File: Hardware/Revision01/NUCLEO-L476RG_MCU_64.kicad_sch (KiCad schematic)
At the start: 56 parts, among them U10 MCU_LQFP64, X2 ABS25-32.768KHZ-6-T, X3 8MHz(16pF)[N/A]

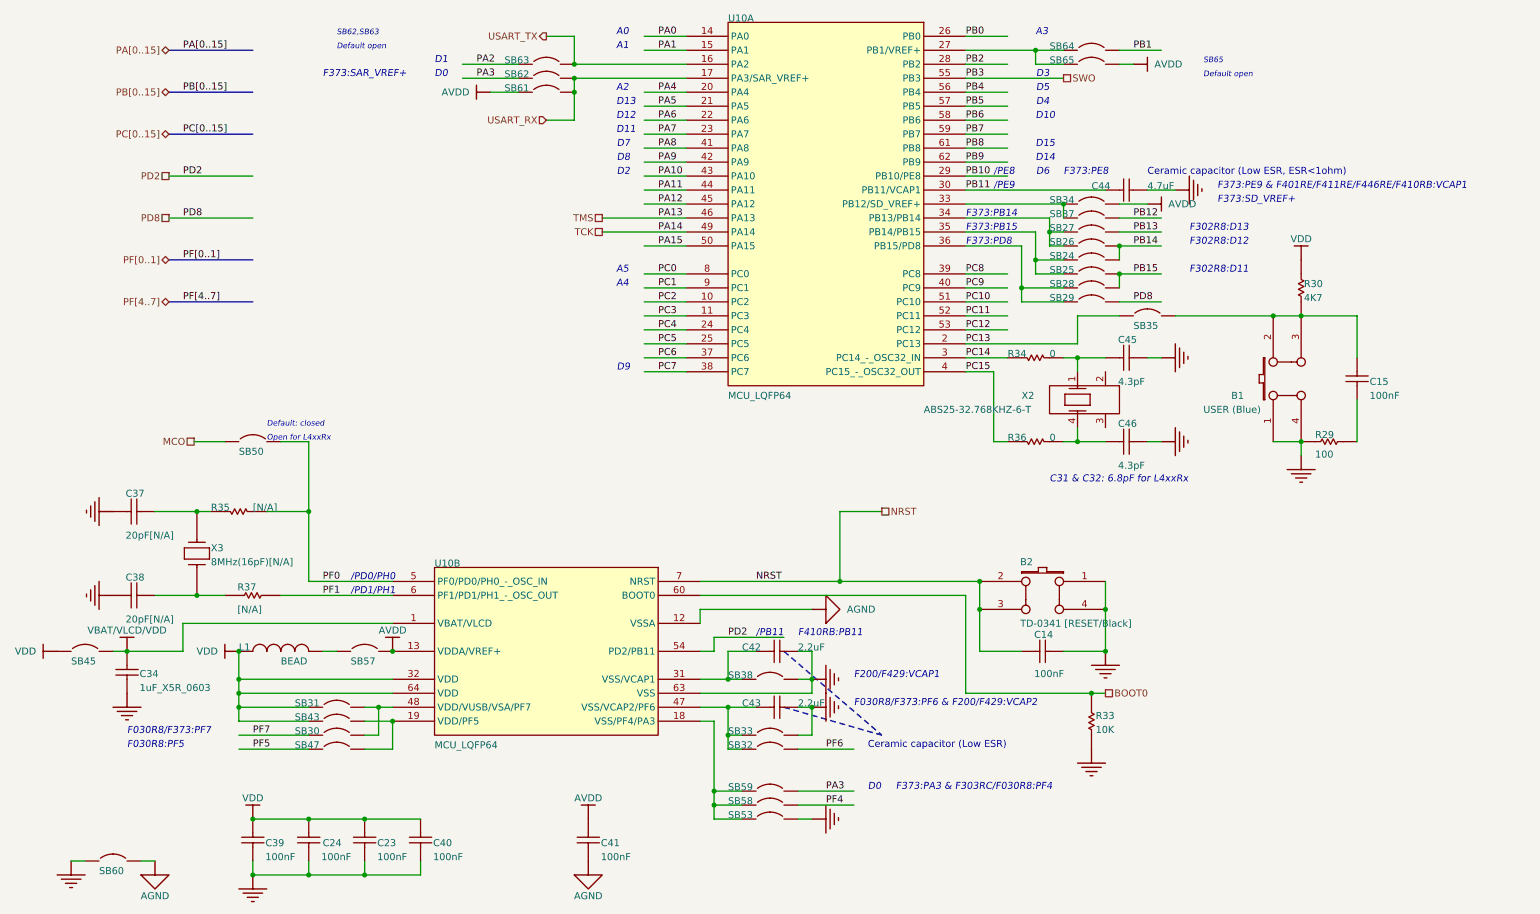
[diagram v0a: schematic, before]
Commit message: . Renamed schematic files, removed old symbol files
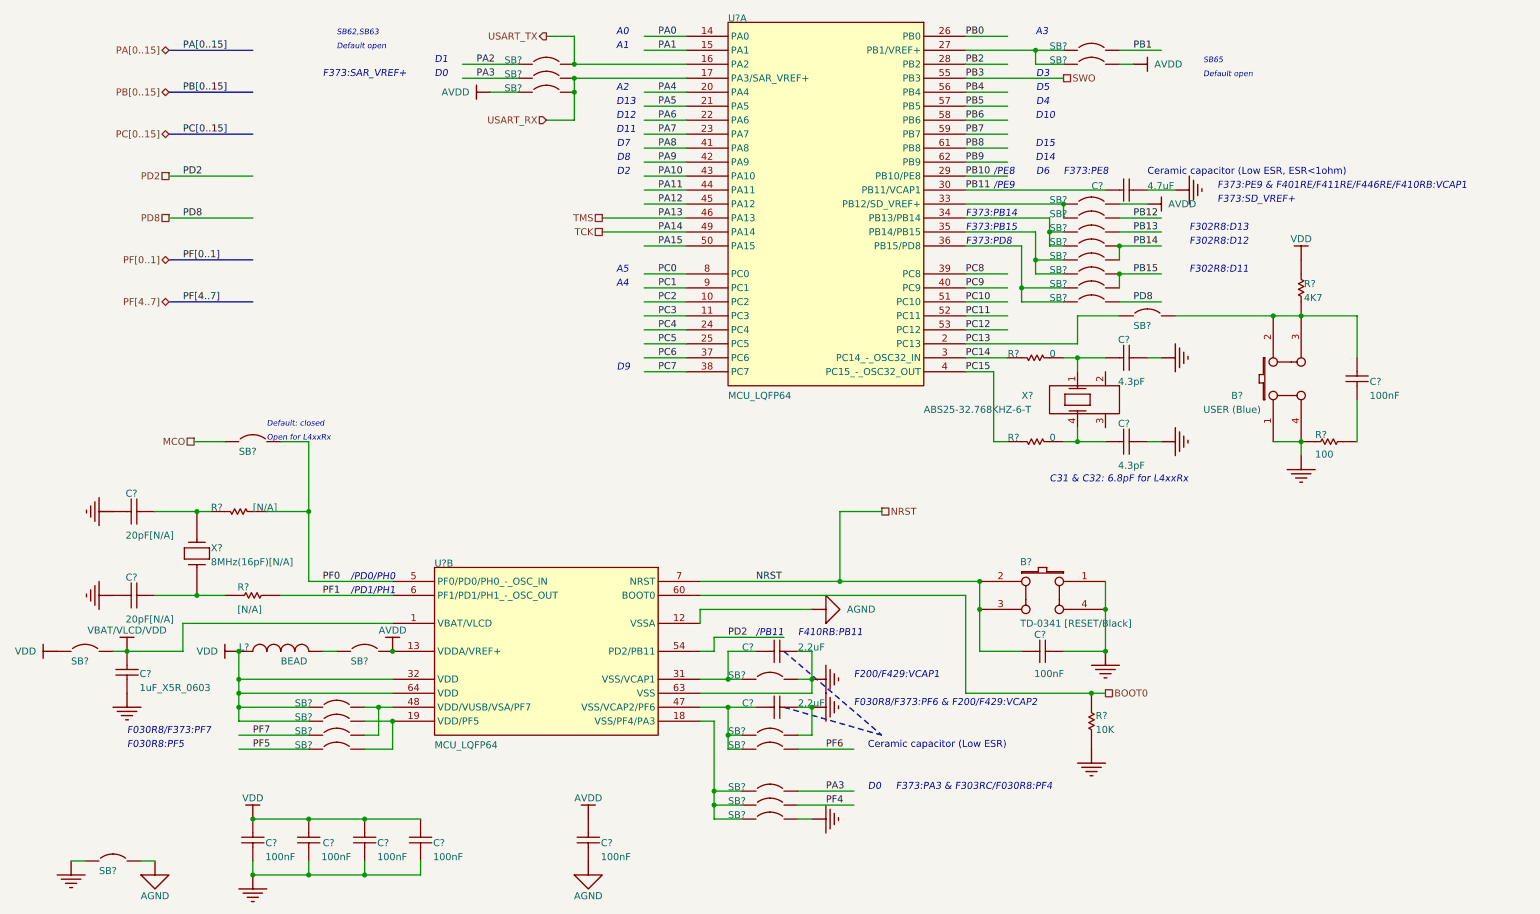
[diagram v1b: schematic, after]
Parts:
- renumbered B2 to B?, B1 to B?, C37 to C?, C45 to C?, C44 to C?, C39 to C?, C34 to C?, C46 to C?, C43 to C?, C14 to C?, C41 to C?, C15 to C?, C24 to C?, C40 to C?, C38 to C?, C23 to C?, C42 to C?, L1 to L?, R29 to R?, R37 to R?, R35 to R?, R34 to R?, R36 to R?, R33 to R?, R30 to R?, SB32 to SB?, SB61 to SB?, SB59 to SB?, SB25 to SB?, SB31 to SB?, SB37 to SB?, SB29 to SB?, SB63 to SB?, SB50 to SB?, SB38 to SB?, SB30 to SB?, SB35 to SB?, SB64 to SB?, SB58 to SB?, SB45 to SB?, SB33 to SB?, SB43 to SB?, SB57 to SB?, SB62 to SB?, SB28 to SB?, SB26 to SB?, SB60 to SB?, SB27 to SB?, SB53 to SB?, SB65 to SB?, SB47 to SB?, SB34 to SB?, SB24 to SB?, U10 to U?, X2 to X?, X3 to X?

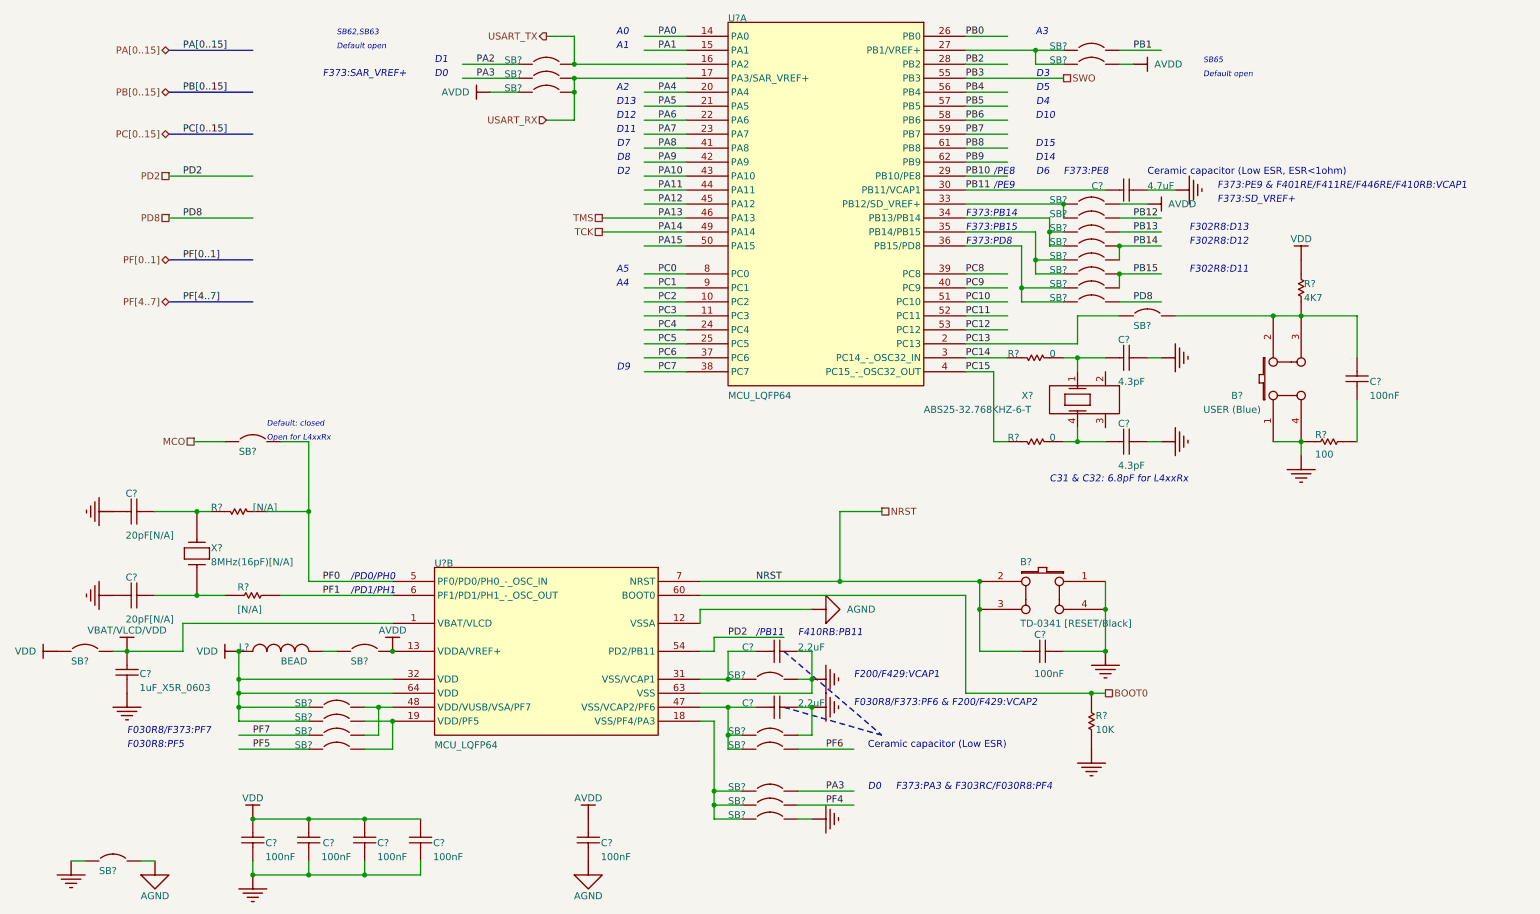
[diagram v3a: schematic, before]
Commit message: . Completed MCU schematic & imported hierarchical model pins
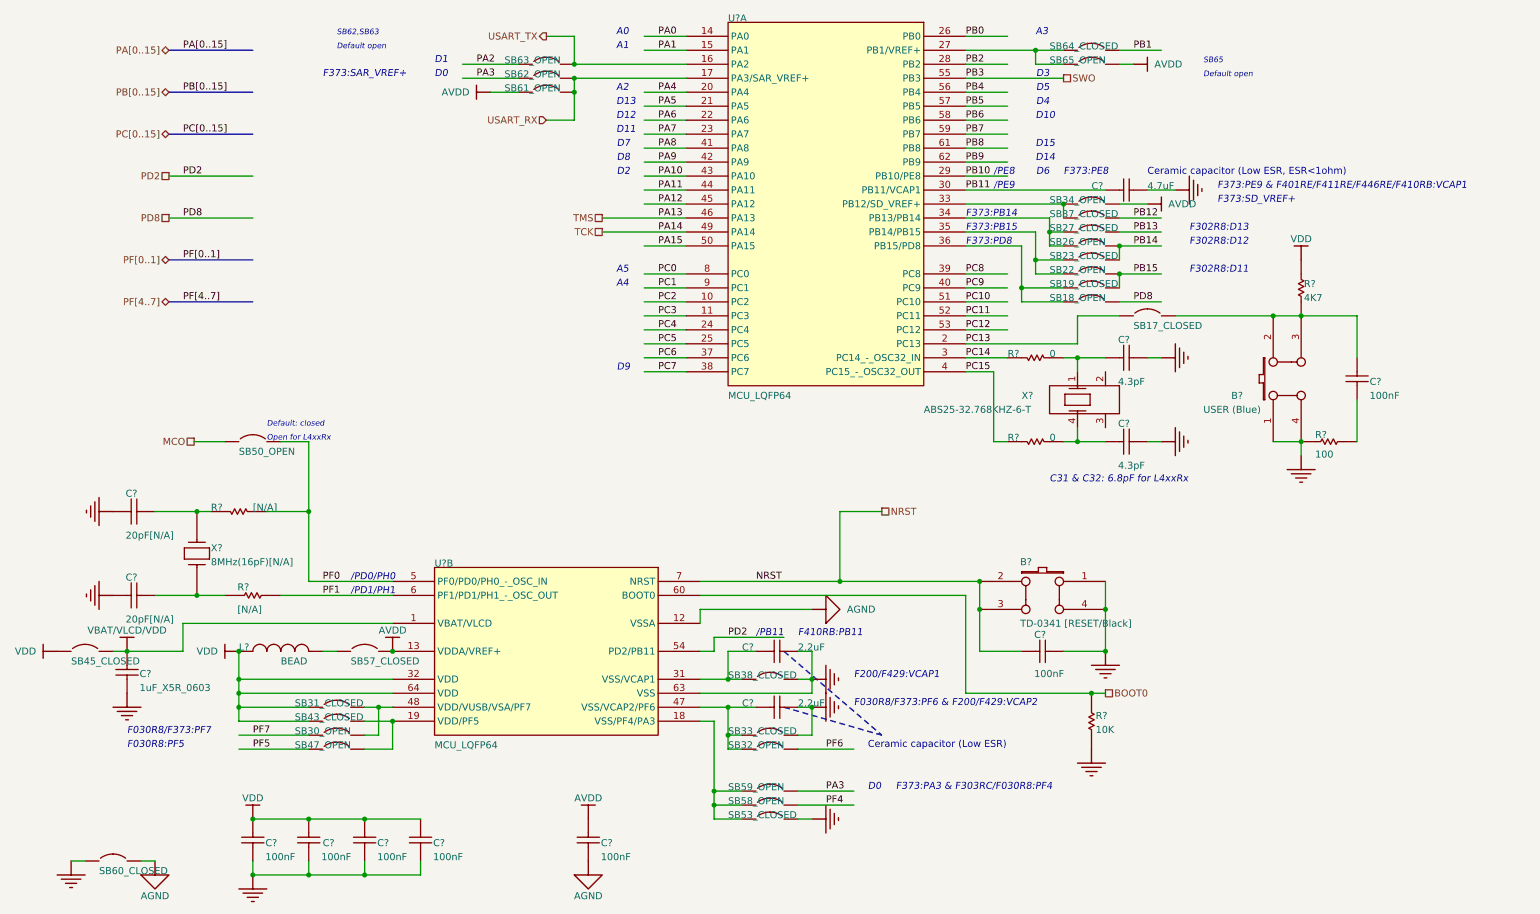
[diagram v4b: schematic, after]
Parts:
- gave numbers to parts that had none: 28

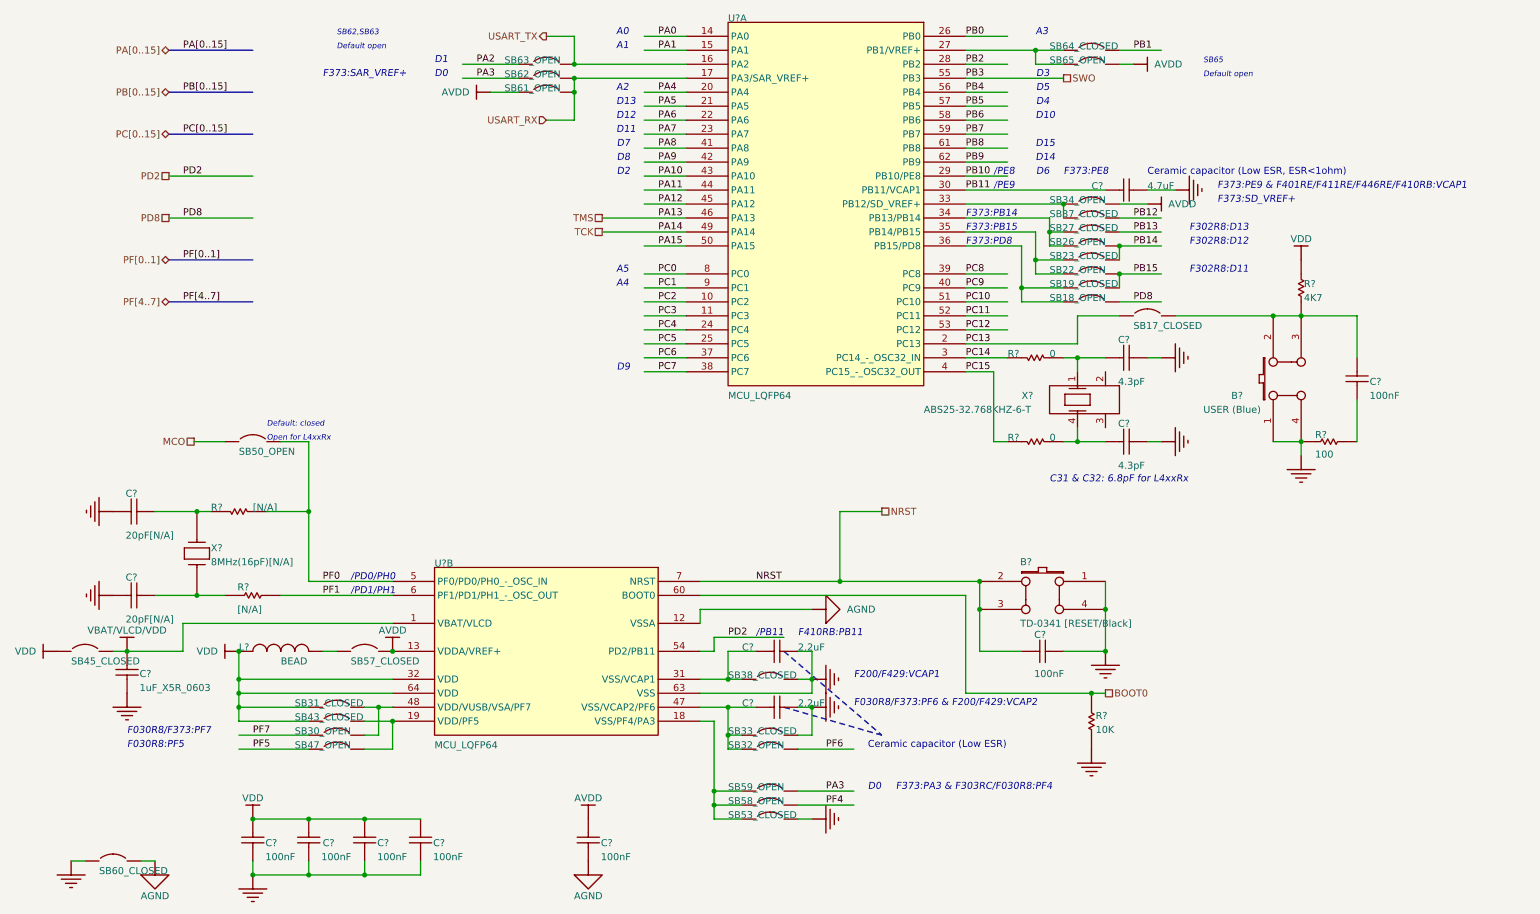
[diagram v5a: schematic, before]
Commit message: CREATE STM32CUBEIDE file to verify all ports Check over CONTROLLER SHEET Improve annotation ordering Move testpoints out of controller sheet
Still performering ERC check
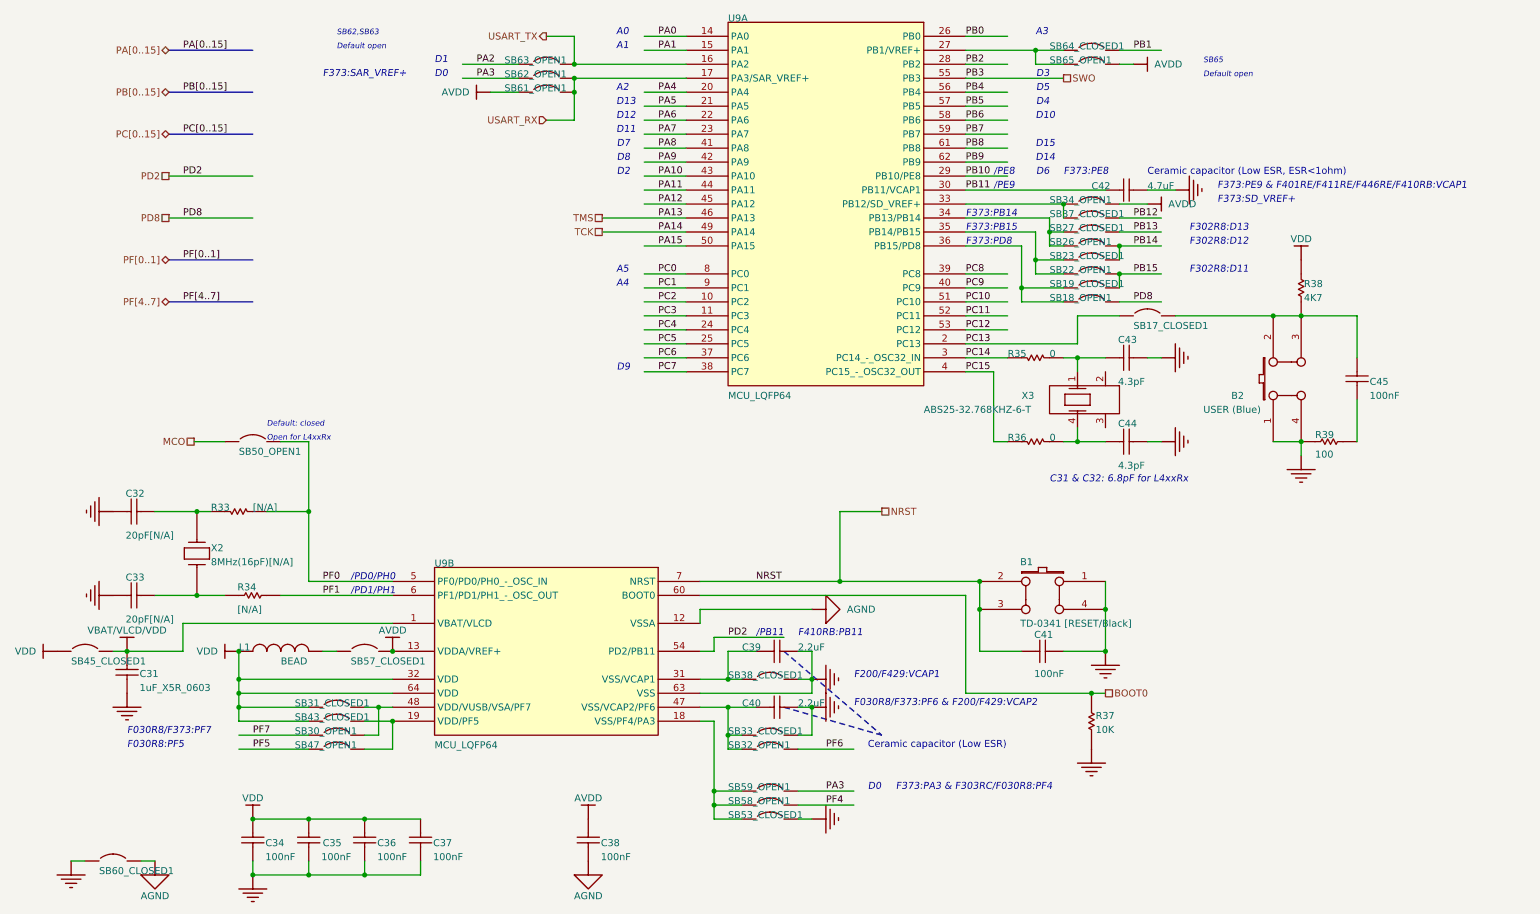
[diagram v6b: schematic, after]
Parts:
- gave numbers to parts that had none: 28
- renumbered SB17_CLOSED to SB17_CLOSED1, SB18_OPEN to SB18_OPEN1, SB19_CLOSED to SB19_CLOSED1, SB22_OPEN to SB22_OPEN1, SB23_CLOSED to SB23_CLOSED1, SB26_OPEN to SB26_OPEN1, SB27_CLOSED to SB27_CLOSED1, SB30_OPEN to SB30_OPEN1, SB31_CLOSED to SB31_CLOSED1, SB32_OPEN to SB32_OPEN1, SB33_CLOSED to SB33_CLOSED1, SB34_OPEN to SB34_OPEN1, SB37_CLOSED to SB37_CLOSED1, SB38_CLOSED to SB38_CLOSED1, SB43_CLOSED to SB43_CLOSED1, SB45_CLOSED to SB45_CLOSED1, SB47_OPEN to SB47_OPEN1, SB50_OPEN to SB50_OPEN1, SB53_CLOSED to SB53_CLOSED1, SB57_CLOSED to SB57_CLOSED1, SB58_OPEN to SB58_OPEN1, SB59_OPEN to SB59_OPEN1, SB60_CLOSED to SB60_CLOSED1, SB61_OPEN to SB61_OPEN1, SB62_OPEN to SB62_OPEN1, SB63_OPEN to SB63_OPEN1, SB64_CLOSED to SB64_CLOSED1, SB65_OPEN to SB65_OPEN1
